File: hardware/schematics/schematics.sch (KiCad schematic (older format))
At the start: 8 parts

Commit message: 5 power supply schematics drawn
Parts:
- removed C? (x4): CP, symbol Device:CP
- removed D? (x2): 1N4001, Diode_THT:D_DO-41_SOD81_P10.16mm_Horizontal, symbol Diode:1N4001
- removed J?: Jack-DC, symbol Connector:Jack-DC
- removed U?: L7805, symbol Regulator_Linear:L7805
- added C1, C4: 0.1U, Capacitor_THT:C_Disc_D3.0mm_W1.6mm_P2.50mm, symbol Device:CP
- added C2: 10U/25V, Capacitor_THT:CP_Radial_D5.0mm_P2.50mm, symbol Device:CP
- added C3: 220U/6V, Capacitor_THT:CP_Radial_D6.3mm_P2.50mm, symbol Device:CP
- added D1, D2: D, Diode_THT:D_A-405_P7.62mm_Horizontal, symbol Device:D
- added F1: Fuse, Capacitor_THT:C_Disc_D7.5mm_W2.5mm_P5.00mm, symbol Device:Fuse
- added J1: Jack-DC, Connector_BarrelJack:BarrelJack_Horizontal, symbol Connector:Jack-DC
- added U1: L7805, Package_TO_SOT_THT:TO-220-3_Vertical, symbol Regulator_Linear:L7805
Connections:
- net labels removed: +9V
- wire segments 27 -> 36
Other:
- note added: "5V Power Supply"
- note added: "Move this to max"

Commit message: Boost converter schematic created
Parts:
- added C1: 47U/25V, Capacitor_THT:CP_Radial_D5.0mm_P2.50mm, symbol Device:CP
- added C4: 33U/100V, Capacitor_THT:CP_Radial_D6.3mm_P2.50mm, symbol Device:CP
- added C6: 0.1U, Capacitor_THT:C_Disc_D3.0mm_W1.6mm_P2.50mm, symbol Device:CP
- added D2: MBR160, Diode_THT:D_A-405_P7.62mm_Horizontal, symbol Device:D_Schottky
- added D3: D_Zener, Diode_THT:D_A-405_P7.62mm_Horizontal, symbol Device:D_Zener
- added L1: 2220U, Inductor_THT:L_Radial_D9.5mm_P5.00mm_Fastron_07HVP, symbol Device:L
- added Q1: Q_NMOS_DGS, Package_DIP:DIP-4_W7.62mm, symbol Device:Q_NMOS_DGS
- D1: value D -> MBR160; symbol Device:D -> Device:D_Schottky
- D4: renamed from D2; value D -> MBR160; symbol Device:D -> Device:D_Schottky
- F1: footprint Capacitor_THT:C_Disc_D7.5mm_W2.5mm_P5.00mm -> Capacitor_THT:C_Disc_D7.5mm_W4.4mm_P5.00mm
- renumbered C1 to C2, C2 to C3, C3 to C5, C4 to C7
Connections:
- net labels added: +9V, PWM, VCC, Vdrive
- net labels removed: +5V
- wire segments 36 -> 66
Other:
- note added: "Boost Converter"
- note added: "Okay to use same?"

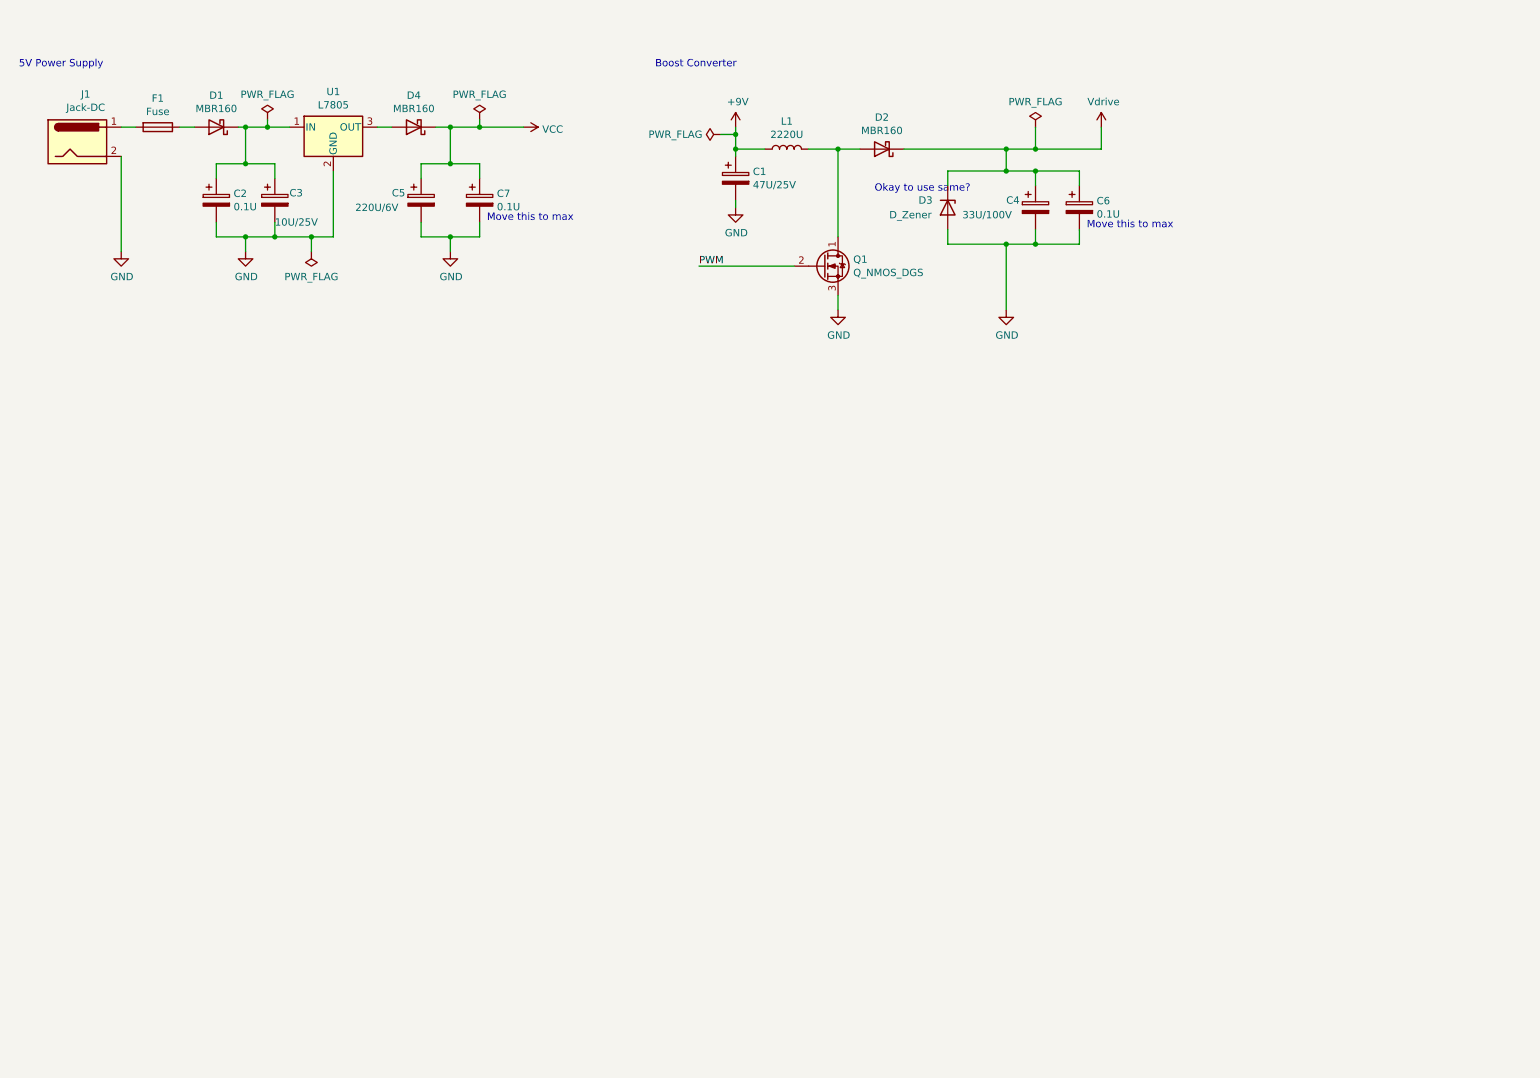
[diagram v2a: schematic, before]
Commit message: Schematic footprints created
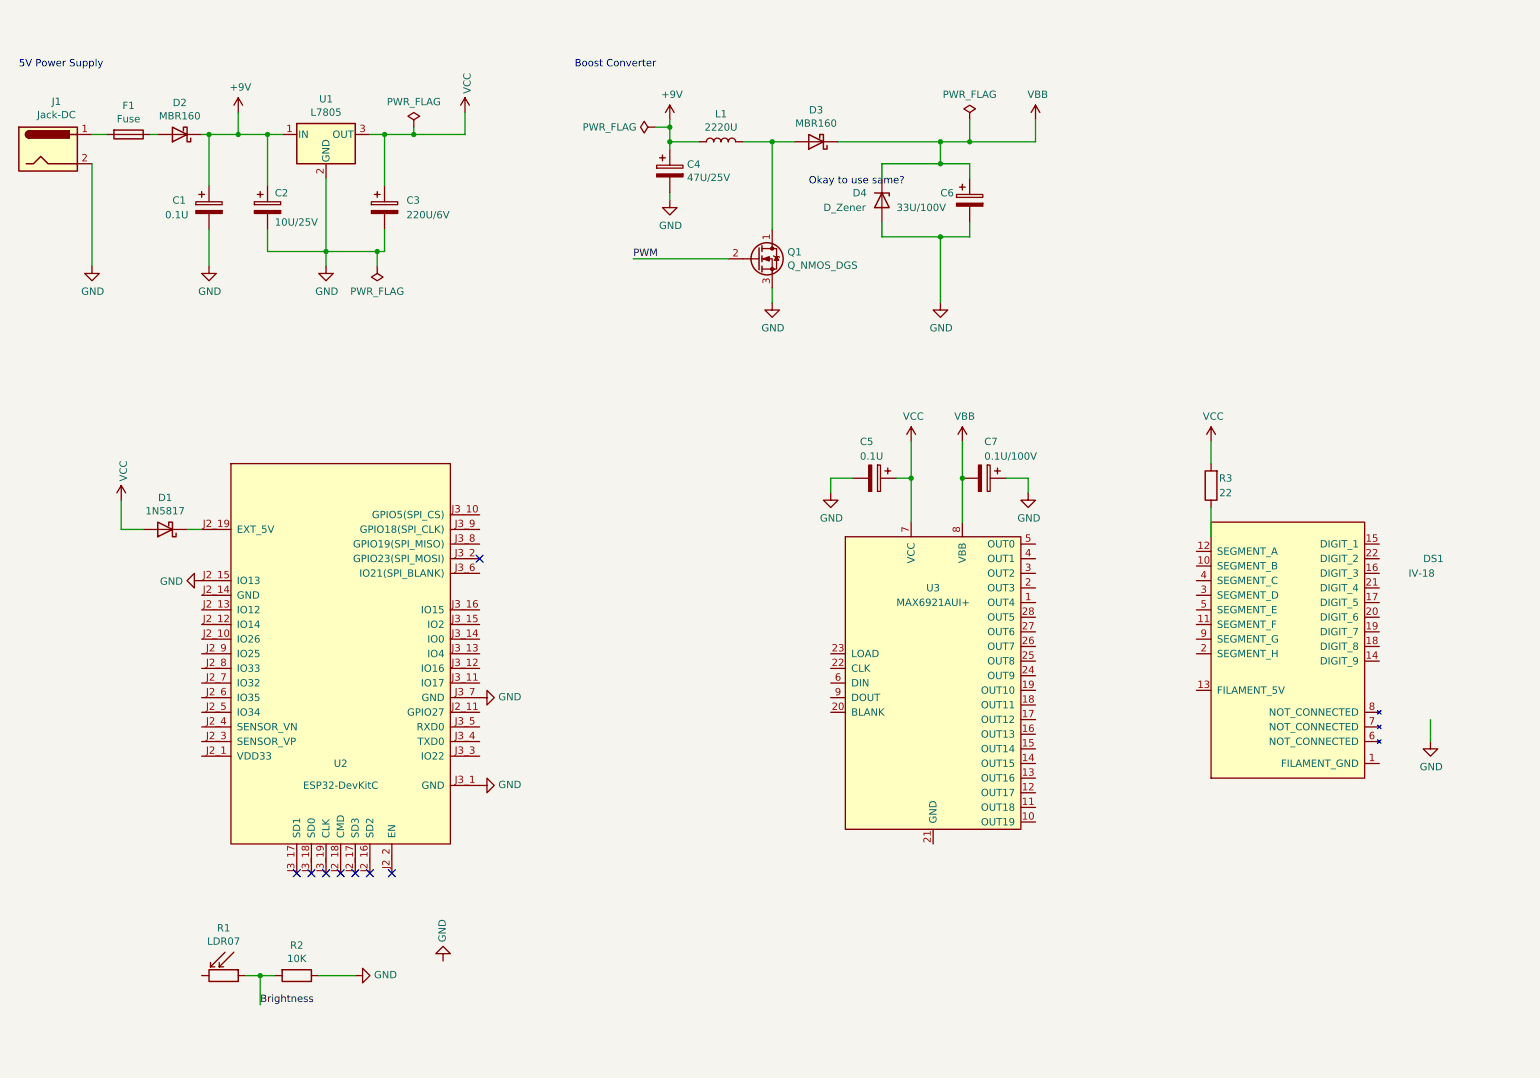
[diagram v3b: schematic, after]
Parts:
- added DS1: IV-18, Connector_PinHeader_1.27mm:PinHeader_2x10_P1.27mm_Vertical, symbol callisto_lib:IV-18
- added R1: LDR07, OptoDevice:R_LDR_5.1x4.3mm_P3.4mm_Vertical, symbol Sensor_Optical:LDR07
- added R2: 10K, Resistor_THT:R_Axial_DIN0309_L9.0mm_D3.2mm_P12.70mm_Horizontal, symbol Device:R
- added R3: 22, Resistor_THT:R_Axial_DIN0309_L9.0mm_D3.2mm_P12.70mm_Horizontal, symbol Device:R
- added U2: ESP32-DevKitC, callisto:ESP32 DevKitC, symbol callisto_lib:ESP32-DevKitC
- added U3: MAX6921AUI+, callisto:MAX6921AUI+, symbol callisto_lib:MAX6921AUI+
- C7: value 0.1U -> 0.1U/100V
- D1: renamed from D4; value MBR160 -> 1N5817
- renumbered C2 to C1, C3 to C2, C5 to C3, C1 to C4, C6 to C5, C4 to C6, D1 to D2, D2 to D3, D3 to D4
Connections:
- net labels added: Brightness, VBB
- net labels removed: Vdrive
- wire segments 66 -> 70
- no-connect marks 0 -> 8
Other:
- note removed: "Move this to max"
- moved on the sheet: C1, C2, C3, C4, C5, C6, C7, D1, D2, D3, D4, F1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

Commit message: Schematics completed
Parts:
- added J2, J3: Conn_01x20, Connector_PinHeader_2.54mm:PinHeader_2x10_P2.54mm_Vertical, symbol Connector_Generic:Conn_01x20
- added TP1: Touchpad, Connector_PinSocket_2.54mm:PinSocket_1x01_P2.54mm_Vertical, symbol callisto_lib:Touchpad
- DS1: footprint Connector_PinHeader_1.27mm:PinHeader_2x10_P1.27mm_Vertical -> callisto:IV-18
- renumbered C5 to C4, C4 to C5, U2 to U1, U1 to U2
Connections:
- net labels added: +3V3, BLANK, BRIGHTNESS, CLK, DIN, LOAD, TOUCH, dig_1, dig_2, dig_3, dig_4, dig_5, dig_6, dig_7, dig_8, dig_9, fil_g, fil_v, seg_a, seg_b, seg_c, seg_d, seg_e, seg_f, seg_g, seg_h
- net labels removed: Brightness
- wire segments 70 -> 157
- no-connect marks 8 -> 33
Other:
- note added: "Light sensor"
- moved on the sheet: C2, C3, C4, C5, C6, C7, D1, D3, D4, DS1, L1, Q1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

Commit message: Main PCB completed
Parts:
- F1: footprint Capacitor_THT:C_Disc_D7.5mm_W4.4mm_P5.00mm -> Fuse:Fuse_Littelfuse_395Series
- J2: footprint Connector_PinHeader_2.54mm:PinHeader_2x10_P2.54mm_Vertical -> Connector_PinSocket_2.54mm:PinSocket_2x10_P2.54mm_Horizontal
- J3: footprint Connector_PinHeader_2.54mm:PinHeader_2x10_P2.54mm_Vertical -> Connector_PinSocket_2.54mm:PinSocket_2x10_P2.54mm_Vertical
- U2: footprint Package_TO_SOT_THT:TO-220-3_Vertical -> Package_TO_SOT_THT:TO-220-3_Horizontal_TabDown
- U3: footprint callisto:MAX6921AUI+ -> Package_SO:TSSOP-28_4.4x9.7mm_P0.65mm
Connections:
- net BRIGHTNESS: now also U1.J2_3 (SENSOR_VP); no longer U1.J2_7 (IO32)
- net GND: now also J2.19 (Pin_19), J2.20 (Pin_20); no longer J2.2 (Pin_2)
- net PWM: now also U1.J2_7 (IO32); no longer U1.J3_12 (IO16)
- net VCC: now also R3.2; no longer R3.1
- net dig_1: no longer J2.12 (Pin_12), U3.25 (OUT8)
- net dig_2: no longer J2.11 (Pin_11), U3.24 (OUT9)
- net dig_3: no longer J2.10 (Pin_10), U3.19 (OUT10)
- net dig_4: no longer J2.9 (Pin_9), U3.18 (OUT11)
- net dig_5: no longer J2.8 (Pin_8), U3.17 (OUT12)
- net dig_6: no longer J2.7 (Pin_7), U3.16 (OUT13)
- net dig_7: no longer J2.6 (Pin_6), U3.15 (OUT14)
- net dig_8: no longer J2.5 (Pin_5), U3.14 (OUT15)
- net dig_9: no longer J2.4 (Pin_4), U3.13 (OUT16)
- net fil_v: no longer J2.3 (Pin_3), R3.2
- net seg_a: no longer J2.20 (Pin_20), U3.5 (OUT0)
- net seg_b: no longer J2.19 (Pin_19), U3.4 (OUT1)
- net seg_c: no longer J2.18 (Pin_18), U3.3 (OUT2)
- net seg_d: no longer J2.17 (Pin_17), U3.2 (OUT3)
- net seg_e: no longer J2.16 (Pin_16), U3.1 (OUT4)
- net seg_f: no longer J2.15 (Pin_15), U3.28 (OUT5)
- net seg_g: no longer J2.14 (Pin_14), U3.27 (OUT6)
- net seg_h: no longer J2.13 (Pin_13), U3.26 (OUT7)
- net O_19: now reaches U3.10 (OUT19)
- net O_19: now also J2.11 (Pin_11)
- net O_18: now reaches U3.11 (OUT18)
- net O_18: now also J2.13 (Pin_13)
- net O_17: now reaches U3.12 (OUT17)
- net O_17: now also J2.15 (Pin_15)
- net at J2.1 (Pin_1): now also R3.1
- new net O_0: J2.18 (Pin_18), U3.5 (OUT0)
- new net O_1: J2.16 (Pin_16), U3.4 (OUT1)
- new net O_10: J2.9 (Pin_9), U3.19 (OUT10)
- new net O_11: J2.7 (Pin_7), U3.18 (OUT11)
- new net O_12: J2.5 (Pin_5), U3.17 (OUT12)
- new net O_13: J2.3 (Pin_3), U3.16 (OUT13)
- new net O_16: J2.17 (Pin_17), U3.13 (OUT16)
- new net O_2: J2.14 (Pin_14), U3.3 (OUT2)
- new net O_3: J2.12 (Pin_12), U3.2 (OUT3)
- new net O_4: J2.10 (Pin_10), U3.1 (OUT4)
- new net O_5: J2.8 (Pin_8), U3.28 (OUT5)
- new net O_6: J2.6 (Pin_6), U3.27 (OUT6)
- new net O_7: J2.4 (Pin_4), U3.26 (OUT7)
- new net O_8: J2.2 (Pin_2), U3.25 (OUT8)
- no-connect marks 33 -> 31
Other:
- moved on the sheet: R3

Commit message: Tube PCB wired
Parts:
- J2: footprint Connector_PinSocket_2.54mm:PinSocket_2x10_P2.54mm_Horizontal -> Connector_PinSocket_2.54mm:PinSocket_2x10_P2.54mm_Vertical
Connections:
- net GND: now also J2.1 (Pin_1); no longer DS1.1 (FILAMENT_GND), J2.19 (Pin_19), J3.2 (Pin_2)
- net dig_1: now also J3.15 (Pin_15); no longer J3.12 (Pin_12)
- net dig_2: now also J3.1 (Pin_1); no longer J3.11 (Pin_11)
- net dig_3: now also J3.13 (Pin_13); no longer J3.10 (Pin_10)
- net dig_4: now also J3.3 (Pin_3); no longer J3.9 (Pin_9)
- net dig_5: now also J3.11 (Pin_11); no longer J3.8 (Pin_8)
- net dig_6: now also J3.5 (Pin_5); no longer J3.7 (Pin_7)
- net dig_7: now also J3.7 (Pin_7); no longer J3.6 (Pin_6)
- net dig_8: now also J3.9 (Pin_9); no longer J3.5 (Pin_5)
- net dig_9: now also J3.17 (Pin_17); no longer J3.4 (Pin_4)
- net fil_v: now also J3.20 (Pin_20); no longer J3.3 (Pin_3)
- net seg_a: now also J3.12 (Pin_12); no longer J3.20 (Pin_20)
- net seg_b: now also J3.16 (Pin_16); no longer J3.19 (Pin_19)
- net seg_c: now also J3.6 (Pin_6); no longer J3.18 (Pin_18)
- net seg_d: now also J3.8 (Pin_8); no longer J3.17 (Pin_17)
- net seg_e: now also J3.4 (Pin_4); no longer J3.16 (Pin_16)
- net seg_f: now also J3.14 (Pin_14); no longer J3.15 (Pin_15)
- net seg_g: now also J3.18 (Pin_18); no longer J3.14 (Pin_14)
- net seg_h: now also J3.10 (Pin_10); no longer J3.13 (Pin_13)
- net at R3.1: now also J2.19 (Pin_19); no longer J2.1 (Pin_1)
- new net fil_g: DS1.1 (FILAMENT_GND), J3.2 (Pin_2)
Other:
- moved on the sheet: J2, R3
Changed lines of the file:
@@
 L Connector_Generic:Conn_01x20 J2
 U 1 1 6121F2BF
-P 7350 4750
-F 0 "J2" H 7350 5900 50  0000 C CNN
-F 1 "Conn_01x20" H 7350 5800 50  0000 C CNN
-F 2 "Connector_PinSocket_2.54mm:PinSocket_2x10_P2.54mm_Horizontal" H 7350 4750 50  0001 C CNN
-F 3 "~" H 7350 4750 50  0001 C CNN
-	1    7350 4750
+P 7450 4750
+F 0 "J2" H 7450 5900 50  0000 C CNN
+F 1 "Conn_01x20" H 7450 5800 50  0000 C CNN
+F 2 "Connector_PinSocket_2.54mm:PinSocket_2x10_P2.54mm_Vertical" H 7450 4750 50  0001 C CNN
+F 3 "~" H 7450 4750 50  0001 C CNN
+	1    7450 4750
 	1    0    0    -1
 $EndComp
@@
 L power:VCC #PWR019
 U 1 1 6117890B
-P 6900 3400
-F 0 "#PWR019" H 6900 3250 50  0001 C CNN
-F 1 "VCC" H 6915 3573 50  0000 C CNN
-F 2 "" H 6900 3400 50  0001 C CNN
-F 3 "" H 6900 3400 50  0001 C CNN
-	1    6900 3400
+P 6850 5200
+F 0 "#PWR019" H 6850 5050 50  0001 C CNN
+F 1 "VCC" H 6865 5373 50  0000 C CNN
+F 2 "" H 6850 5200 50  0001 C CNN
+F 3 "" H 6850 5200 50  0001 C CNN
+	1    6850 5200
 	1    0    0    -1
 $EndComp
@@
 L Device:R R3
 U 1 1 610C9DA0
-P 6900 3650
-F 0 "R3" H 6800 3600 50  0000 C CNN
-F 1 "22" H 6800 3700 50  0000 C CNN
-F 2 "Resistor_THT:R_Axial_DIN0309_L9.0mm_D3.2mm_P12.70mm_Horizontal" V 6830 3650 50  0001 C CNN
-F 3 "~" H 6900 3650 50  0001 C CNN
-	1    6900 3650
+P 6850 5450
+F 0 "R3" H 6750 5400 50  0000 C CNN
+F 1 "22" H 6750 5500 50  0000 C CNN
+F 2 "Resistor_THT:R_Axial_DIN0309_L9.0mm_D3.2mm_P12.70mm_Horizontal" V 6780 5450 50  0001 C CNN
+F 3 "~" H 6850 5450 50  0001 C CNN
+	1    6850 5450
 	-1   0    0    1
 $EndComp
@@
 Wire Wire Line
 	10500 4900 10900 4900
-Text Label 8000 3850 0    50   ~ 0
-seg_a
-Text Label 8000 3950 0    50   ~ 0
-seg_b
-Text Label 8000 4050 0    50   ~ 0
-seg_c
-Text Label 8000 4150 0    50   ~ 0
-seg_d
-Text Label 8000 4250 0    50   ~ 0
-seg_e
-Text Label 8000 4350 0    50   ~ 0
-seg_f
-Text Label 8000 4450 0    50   ~ 0
-seg_g
-Text Label 8000 4550 0    50   ~ 0
-seg_h
-Text Label 8000 4650 0    50   ~ 0
-dig_1
-Text Label 8000 4750 0    50   ~ 0
-dig_2
-Text Label 8000 4850 0    50   ~ 0
-dig_3
-Text Label 8000 4950 0    50   ~ 0
-dig_4
-Text Label 8000 5050 0    50   ~ 0
-dig_5
-Text Label 8000 5150 0    50   ~ 0
-dig_6
-Text Label 8000 5250 0    50   ~ 0
-dig_7
-Text Label 8000 5350 0    50   ~ 0
-dig_8
-Text Label 8000 5450 0    50   ~ 0
-dig_9
 Wire Wire Line
 	8000 3850 8350 3850
@@
 	8350 3850 8450 3750
 Wire Wire Line
-	8000 3950 8350 3950
-Entry Wire Line
-	8350 3950 8450 3850
-Wire Wire Line
 	8000 4050 8350 4050
 Entry Wire Line
@@
 Entry Wire Line
 	8350 5450 8450 5350
-Text Label 8000 5550 0    50   ~ 0
-fil_v
 Wire Wire Line
 	8000 5550 8350 5550
 Entry Wire Line
 	8350 5550 8450 5450
-Text Label 8000 5650 0    50   ~ 0
-fil_g
 Wire Wire Line
 	8000 5650 8350 5650
 Entry Wire Line
 	8350 5650 8450 5550
-NoConn ~ 8000 5750
 Text Label 9000 5100 0    50   ~ 0
 fil_v
@@
 	6850 5750 6850 6250
 Wire Wire Line
-	6850 5750 7150 5750
+	6850 5750 7250 5750
 Wire Wire Line
 	1200 1400 1200 1850
@@
 	3550 4150 4000 4150
 Wire Wire Line
-	6900 3400 6900 3500
-Wire Wire Line
-	6900 3850 7150 3850
-Wire Wire Line
-	6900 3800 6900 3850
+	6850 5200 6850 5300
+Wire Wire Line
+	6850 5650 7250 5650
+Wire Wire Line
+	6850 5600 6850 5650
 Wire Wire Line
 	1100 5150 1650 5150
@@
 Text Label 6450 3950 0    50   ~ 0
 O_1
-Text Label 7150 5350 2    50   ~ 0
+Text Label 7250 5350 2    50   ~ 0
 O_1
 Text Label 6450 4050 0    50   ~ 0
@@
 Text Label 6450 4350 0    50   ~ 0
 O_5
-Text Label 7150 5150 2    50   ~ 0
+Text Label 7250 5150 2    50   ~ 0
 O_2
-Text Label 7150 4950 2    50   ~ 0
+Text Label 7250 4950 2    50   ~ 0
 O_3
-Text Label 7150 4750 2    50   ~ 0
+Text Label 7250 4750 2    50   ~ 0
 O_4
-Text Label 7150 4550 2    50   ~ 0
+Text Label 7250 4550 2    50   ~ 0
 O_5
 Text Label 6450 3850 0    50   ~ 0
 O_0
-Text Label 7150 5550 2    50   ~ 0
+Text Label 7250 5550 2    50   ~ 0
 O_0
 Text Label 6450 4450 0    50   ~ 0
@@
 Text Label 6450 5750 0    50   ~ 0
 O_19
-Text Label 7150 4350 2    50   ~ 0
+Text Label 7250 4350 2    50   ~ 0
 O_6
-Text Label 7150 4150 2    50   ~ 0
+Text Label 7250 4150 2    50   ~ 0
 O_7
-Text Label 7150 3950 2    50   ~ 0
+Text Label 7250 3950 2    50   ~ 0
 O_8
-Wire Wire Line
-	7150 5650 6850 5650
-Wire Wire Line
-	6850 5650 6850 5750
-Connection ~ 6850 5750
 Text Label 6450 5650 0    50   ~ 0
 O_18
@@
 Text Label 6450 5450 0    50   ~ 0
 O_16
-Text Label 7150 4850 2    50   ~ 0
+Text Label 7250 4850 2    50   ~ 0
 O_19
-Text Label 7150 5050 2    50   ~ 0
+Text Label 7250 5050 2    50   ~ 0
 O_18
-Text Label 7150 5250 2    50   ~ 0
+Text Label 7250 5250 2    50   ~ 0
 O_17
-Text Label 7150 5450 2    50   ~ 0
+Text Label 7250 5450 2    50   ~ 0
 O_16
 Text Label 6450 5150 0    50   ~ 0
@@
 Text Label 6450 4950 0    50   ~ 0
 O_11
-Text Label 7150 4650 2    50   ~ 0
+Text Label 7250 4650 2    50   ~ 0
 O_10
-Text Label 7150 4450 2    50   ~ 0
+Text Label 7250 4450 2    50   ~ 0
 O_11
-Text Label 7150 4250 2    50   ~ 0
+Text Label 7250 4250 2    50   ~ 0
 O_12
-Text Label 7150 4050 2    50   ~ 0
+Text Label 7250 4050 2    50   ~ 0
 O_13
 NoConn ~ 6450 4750
@@
 	1    0    0    -1
 $EndComp
+Wire Wire Line
+	8000 5750 8350 5750
+Entry Wire Line
+	8350 5750 8450 5650
+Text Label 8050 3850 0    50   ~ 0
+fil_v
+Text Label 8050 4150 0    50   ~ 0
+dig_9
+Text Label 8050 4350 0    50   ~ 0
+dig_1
+Text Label 8050 4550 0    50   ~ 0
+dig_3
+Text Label 8050 4750 0    50   ~ 0
+dig_5
+Text Label 8050 4950 0    50   ~ 0
+dig_8
+Text Label 8050 5150 0    50   ~ 0
+dig_7
+Text Label 8050 5350 0    50   ~ 0
+dig_6
+Text Label 8050 5550 0    50   ~ 0
+dig_4
+Text Label 8050 5750 0    50   ~ 0
+dig_2
 $Comp
 L power:GND #PWR0101
-U 1 1 611EEFB0
-P 8350 6250
-F 0 "#PWR0101" H 8350 6000 50  0001 C CNN
-F 1 "GND" H 8355 6077 50  0000 C CNN
-F 2 "" H 8350 6250 50  0001 C CNN
-F 3 "" H 8350 6250 50  0001 C CNN
-	1    8350 6250
-	1    0    0    -1
-$EndComp
-Wire Wire Line
-	8350 6250 8350 5650
+U 1 1 6120D033
+P 6850 3950
+F 0 "#PWR0101" H 6850 3700 50  0001 C CNN
+F 1 "GND" H 6855 3777 50  0000 C CNN
+F 2 "" H 6850 3950 50  0001 C CNN
+F 3 "" H 6850 3950 50  0001 C CNN
+	1    6850 3950
+	1    0    0    -1
+$EndComp
+Wire Wire Line
+	7250 3850 6850 3850
+Wire Wire Line
+	6850 3850 6850 3950
+Text Label 8050 5650 0    50   ~ 0
+fil_g
+NoConn ~ 8000 3950
 Wire Bus Line
 	4650 3200 4650 4900
@@
 	11000 3500 11000 5500
 Wire Bus Line
-	8450 3500 8450 5550
+	8450 3500 8450 5650
+Text Label 8050 4850 0    50   ~ 0
+seg_h
+Text Label 8050 5050 0    50   ~ 0
+seg_d
+Text Label 8050 5250 0    50   ~ 0
+seg_c
+Text Label 8050 5450 0    50   ~ 0
+seg_e
+Text Label 8050 4650 0    50   ~ 0
+seg_a
+Text Label 8050 4450 0    50   ~ 0
+seg_f
+Text Label 8050 4250 0    50   ~ 0
+seg_b
+Text Label 8050 4050 0    50   ~ 0
+seg_g
 $EndSCHEMATC
